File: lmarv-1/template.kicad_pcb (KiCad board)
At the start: 4 copper layers, 158 x 115.2 mm, 120 parts, among them J1 Conn_02x03_Odd_Even, P1 dual-pcie-cardedge_split, U1 74LVC541, U10 74LVC541_a, U11 74LVC541_a, U12 74LVC541_a, U13 74LVC541_a, U14 74LVC541, U15 AT28BV64B-20JU, U16 74LVC541, U17 74LVC541, U18 74LVC541, U19 74LVC541, U2 74LVC04, U20 74LVC541, U21 74LVC541, U22 74LVC541, U23 74LVC541, U24 74LVC541_a, U25 74LVC541_a, U26 74LVC541, U27 74LVC541, U28 IS61LV256AL, U29 IS61LV256AL, U3 74LVC32, U30 IS61LV256AL, U31 IS61LV256AL, U32 IS61LV256AL, U33 IS61LV256AL, U34 IS61LV256AL, U35 AT28BV256B-20JU, U36 AT28BV64B-20JU, U37 74LVC541, U38 74LVC541_a, U39 IS61LV256AL, U4 74HC590, U40 74LVC541, U41 74LVC541, U42 74LVC541, U43 74LVC541, U44 74LVC541, U45 IS61LV256AL, U46 IS61LV256AL, U47 IS61LV256AL, U48 IS61LV256AL, U49 IS61LV256AL, U5 74HC590, U50 IS61LV256AL, U51 IS61LV256AL, U52 IS61LV256AL, U53 74LVC541, U54 74LVC541, U55 74LVC541, U56 74LVC541, U6 74LVC541_a, U7 74LVC541_a, U8 74LVC541_a, U9 74LVC541_a

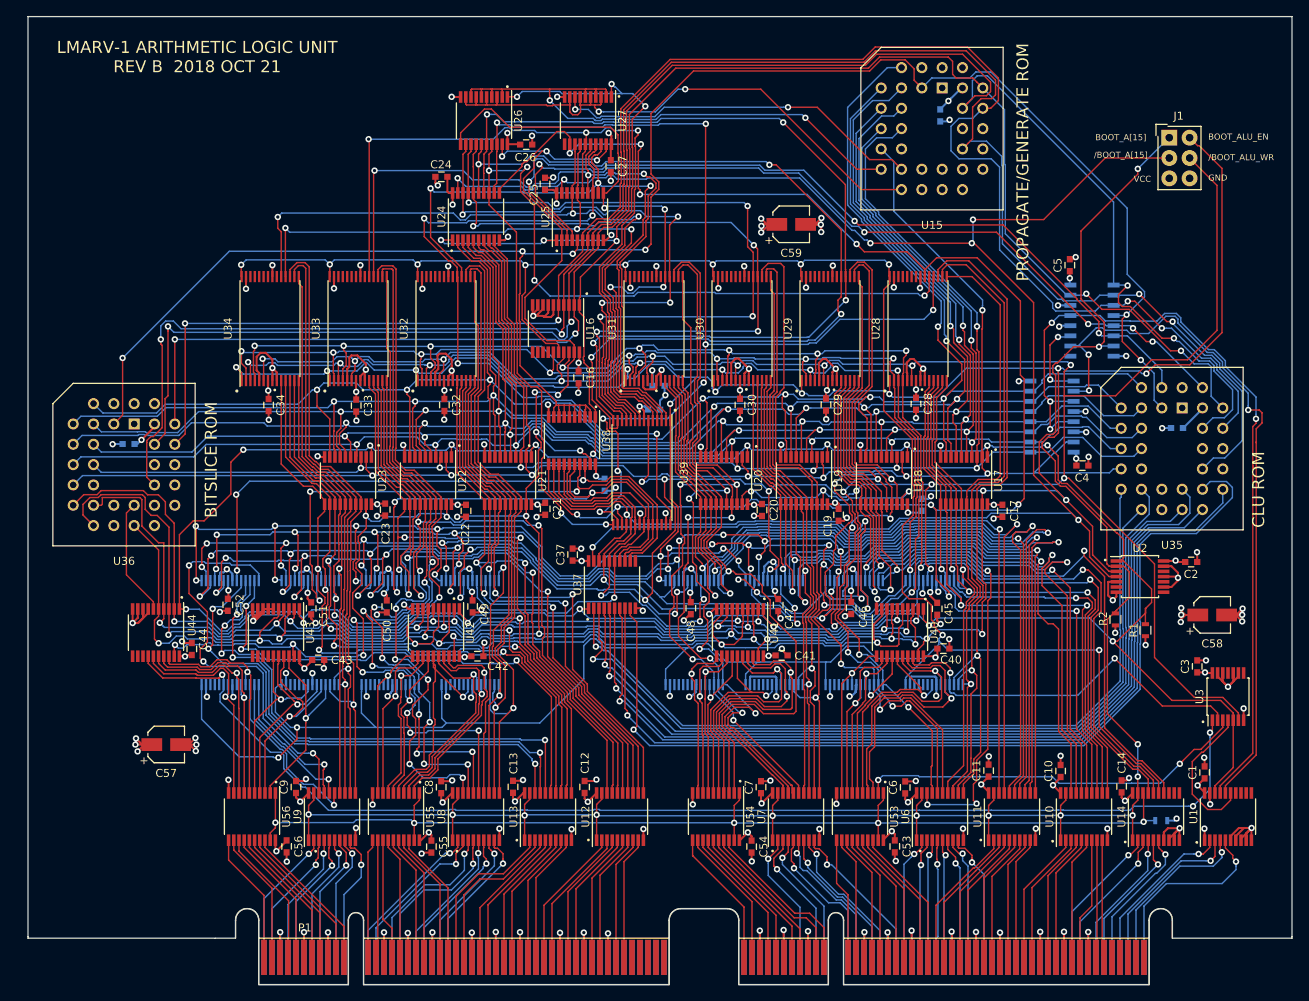
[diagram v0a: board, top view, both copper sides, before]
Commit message: ALU rev D, with simulations
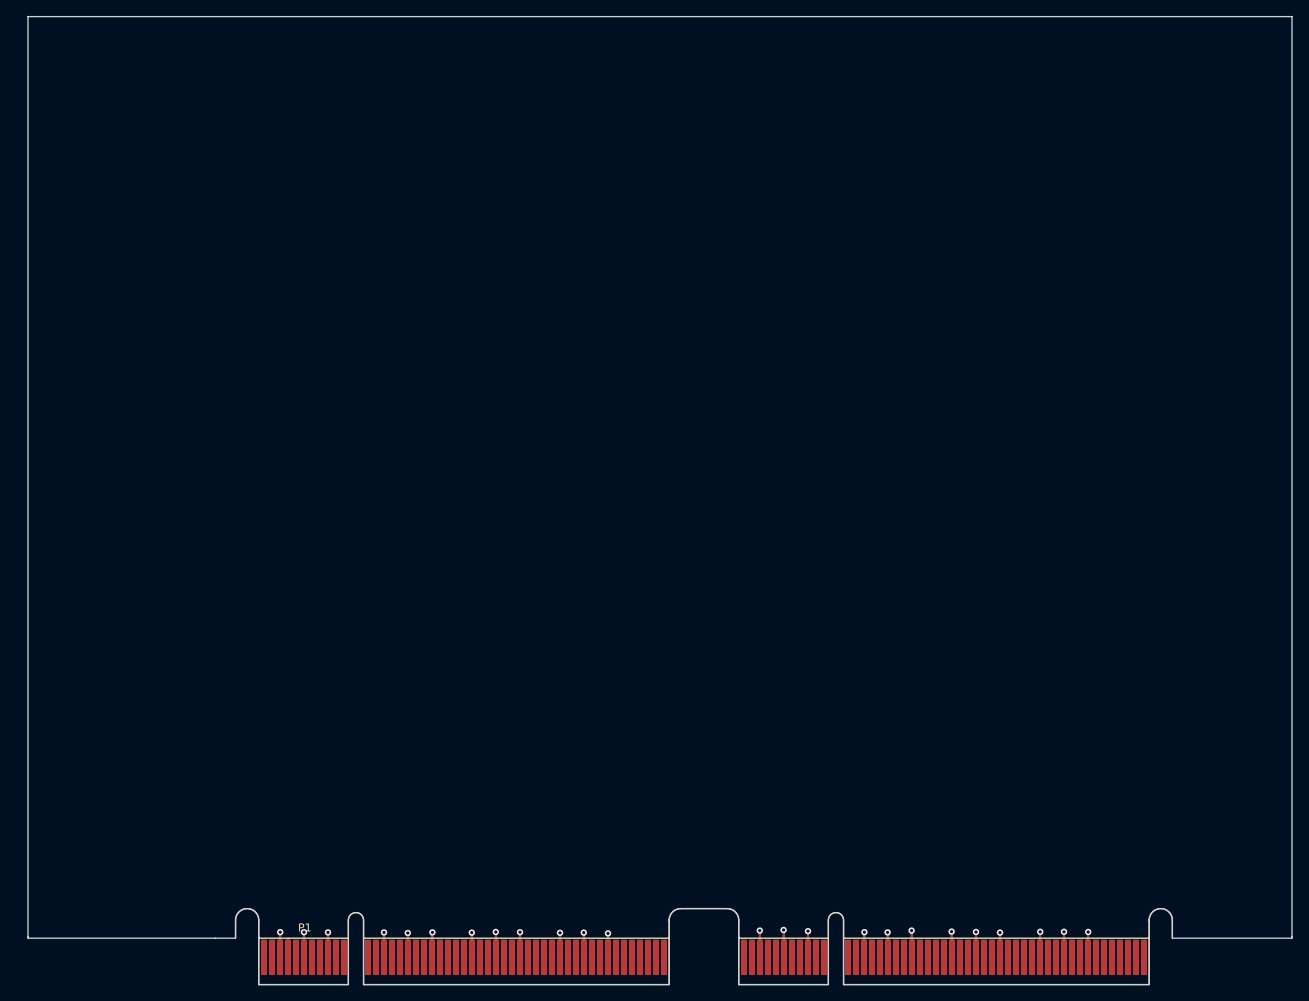
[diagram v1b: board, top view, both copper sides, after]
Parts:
- removed C1, C10, C11, C12, C13, C14, C15, C16, C17, C18, C19, C2, C20, C21, C22, C23, C24, C25, C26, C27, C28, C29, C3, C30, C31, C32, C33, C34, C35, C36, C37, C38, C39, C4, C40, C41, C42, C43, C44, C45, C46, C47, C48, C49, C5, C50, C51, C52, C53, C54, C55, C56, C6, C7, C8, C9: 100n, Capacitors_SMD:C_0603
- removed C57, C58, C59: 1u, Capacitors_SMD:CP_Elec_4x4.5
- removed J1: Conn_02x03_Odd_Even, Connectors_Samtec:SDL-106-X-XX_2x03
- removed R1, R2, R3: 10k, Resistors_SMD:R_0603
- removed U1, U14, U16, U17, U18, U19, U20, U21, U22, U23, U26, U27, U37, U40, U41, U42, U43, U44, U53, U54, U55, U56: 74LVC541, Housings_SSOP:TSSOP-20_4.4x6.5mm_Pitch0.65mm
- removed U10, U11, U12, U13, U24, U25, U38, U6, U7, U8, U9: 74LVC541_a, Housings_SSOP:TSSOP-20_4.4x6.5mm_Pitch0.65mm
- removed U15, U36: AT28BV64B-20JU, Sockets:PLCC32
- removed U2: 74LVC04, Housings_SSOP:TSSOP-14_4.4x5mm_Pitch0.65mm
- removed U28, U29, U30, U31, U32, U33, U34, U39, U45, U46, U47, U48, U49, U50, U51, U52: IS61LV256AL, lmarv:TSOP-I-28_18.4x8mm_Pitch0.55mm
- removed U3: 74LVC32, Housings_SSOP:TSSOP-14_4.4x5mm_Pitch0.65mm
- removed U35: AT28BV256B-20JU, Sockets:PLCC32
- removed U4, U5: 74HC590, Housings_SOIC:SOIC-16_3.9x9.9mm_Pitch1.27mm
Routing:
- net /BOOT_ALU_EN: track 562.4 -> 0.00 mm, vias 35 -> 0
- net /~BOOT_ALU_WR: track 450.4 -> 0.00 mm, vias 28 -> 0
- net /~BOOT_ALU_EN: track 441.6 -> 0.00 mm, vias 23 -> 0
- net /BOOT_A[15]: track 391.7 -> 0.00 mm, vias 25 -> 0
- net GNDREF: track 462.1 -> 101.6 mm, vias 172 -> 16
- net /alu_f[2]: track 348.6 -> 0.00 mm, vias 12 -> 0
- net /alu_f[0]: track 342.2 -> 0.00 mm, vias 26 -> 0
- net /alu_f[1]: track 334.5 -> 0.00 mm, vias 20 -> 0
- net /alu_f[3]: track 333.8 -> 0.00 mm, vias 26 -> 0
- net /BOOT_A[7]: track 274.5 -> 0.00 mm, vias 8 -> 0
- net /BOOT_A[6]: track 258.7 -> 0.00 mm, vias 8 -> 0
- net /BOOT_A[5]: track 257.5 -> 0.00 mm, vias 8 -> 0
- net /BOOT_A[4]: track 244.5 -> 0.00 mm, vias 8 -> 0
- net /BOOT_A[12]: track 240.4 -> 0.00 mm, vias 6 -> 0
- net /BOOT_A[3]: track 238.9 -> 0.00 mm, vias 8 -> 0
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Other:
- board text removed: "/BOOT_ALU_WR"
- board text removed: "/BOOT_A[15]"
- board text removed: "BITSLICE ROM"
- board text removed: "BOOT_ALU_EN"
- board text removed: "BOOT_A[15]"
- board text removed: "CLU ROM"
- board text removed: "GND"
- board text removed: "LMARV-1 ARITHMETIC LOGIC UNIT REV B 2018 OCT 21"
- board text removed: "PROPAGATE/GENERATE ROM"
- board text removed: "VCC"
